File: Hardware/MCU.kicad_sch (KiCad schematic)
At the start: 28 parts, among them J3 SWD, SW1 Reset, SW2 BOOT, U4 STM32L431CBTx, U5 74AHC1G32, Y1 8M

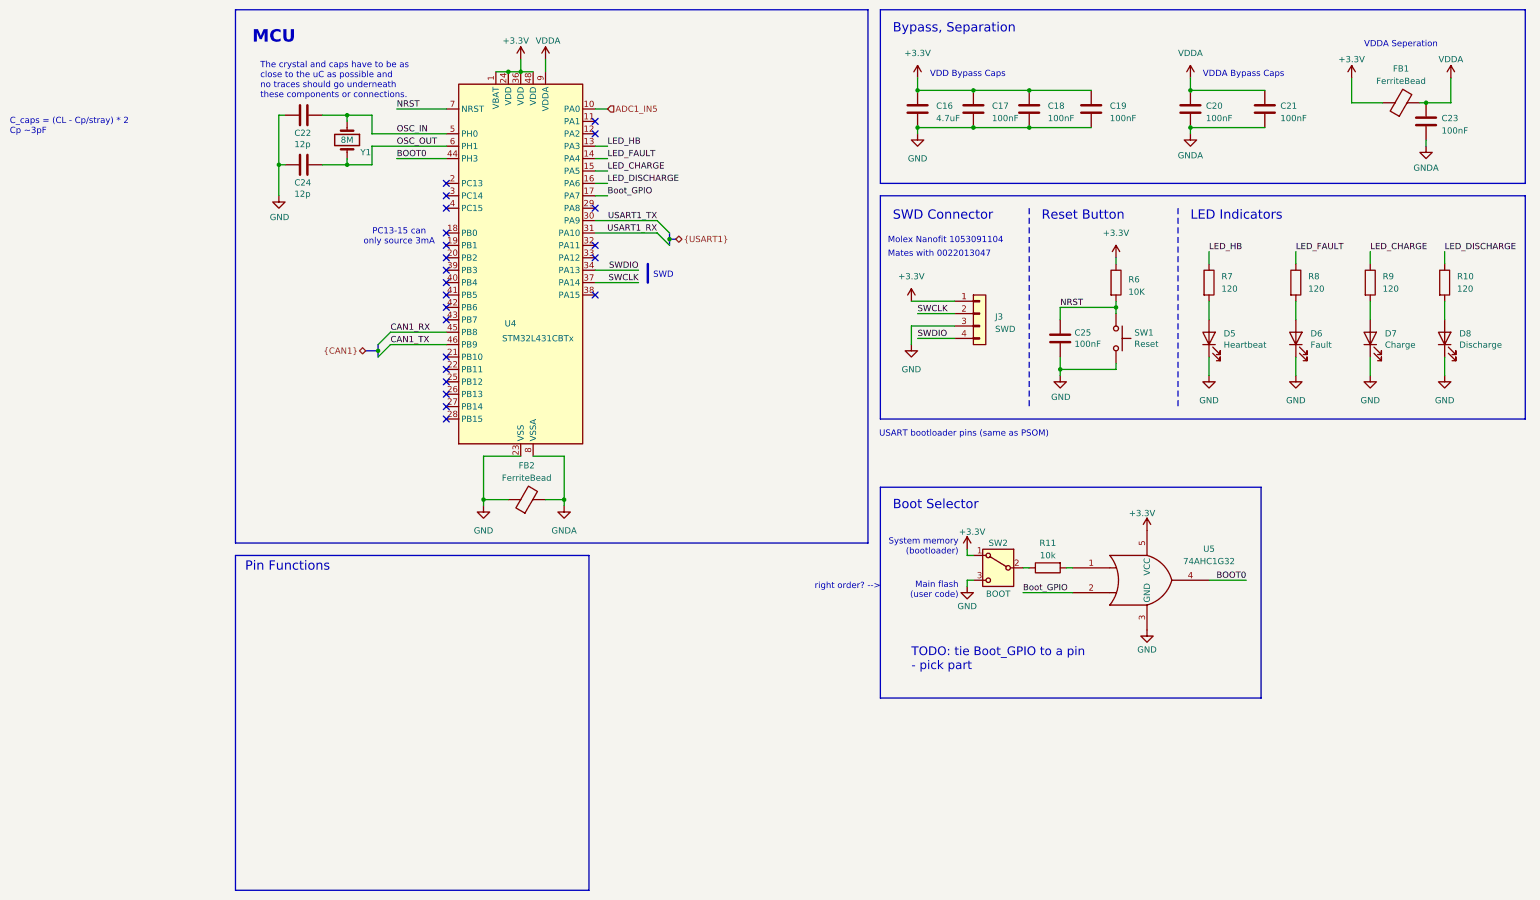
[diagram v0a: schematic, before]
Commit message: changed to 2 channel op amp, stole RPP from PSOM
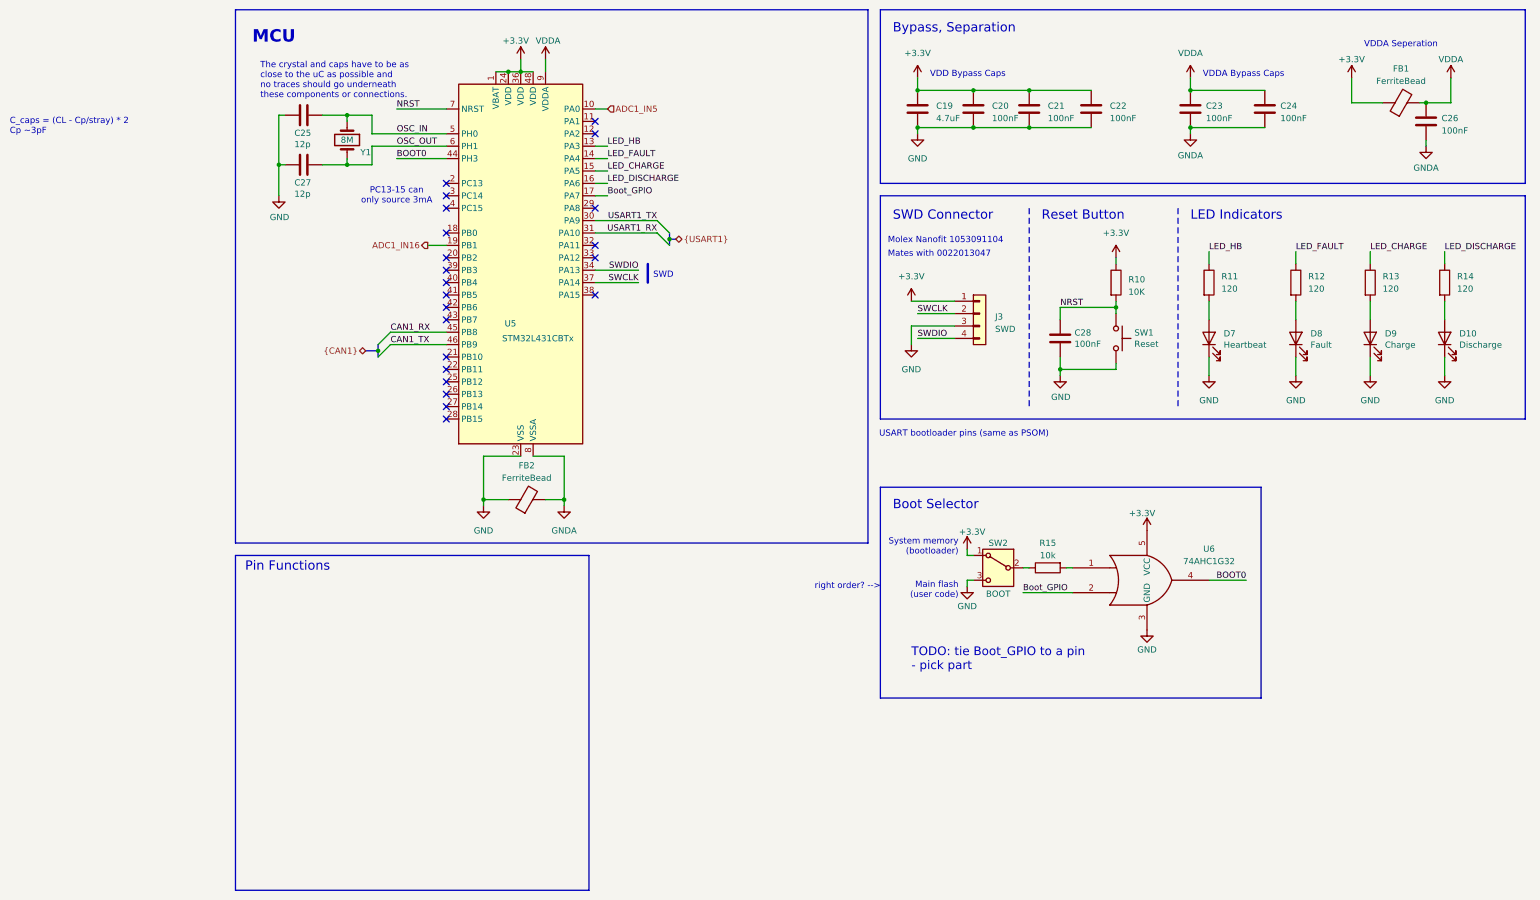
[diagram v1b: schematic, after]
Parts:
- renumbered C16 to C19, C17 to C20, C18 to C21, C19 to C22, C20 to C23, C21 to C24, C22 to C25, C23 to C26, C24 to C27, C25 to C28, D8 to D10, D5 to D7, D6 to D8, D7 to D9, R6 to R10, R7 to R11, R8 to R12, R9 to R13, R10 to R14, R11 to R15, U4 to U5, U5 to U6
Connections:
- net ADC1_IN16: now reaches U5.19 (PB1)
- no-connect marks 23 -> 22

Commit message: added voltage reference, shunt model; addressed comments
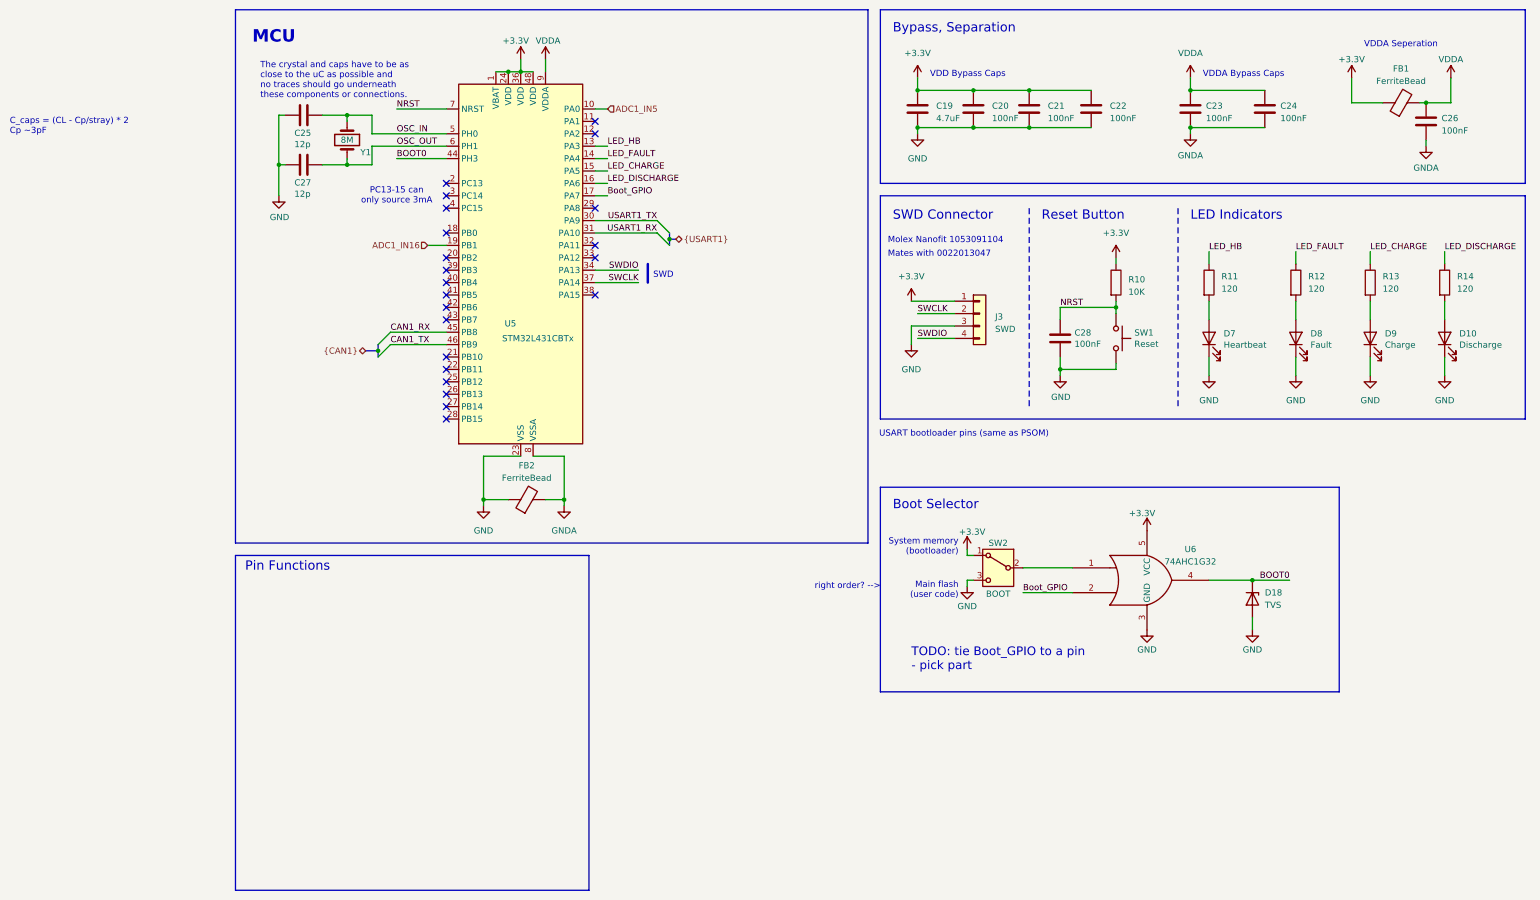
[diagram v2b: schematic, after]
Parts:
- removed R15: 10k, Resistor_SMD:R_0603_1608Metric_Pad0.98x0.95mm_HandSolder, symbol Device:R
- added D18: TVS, Diode_SMD:D_SOD-123F, symbol Device:D_Zener
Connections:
- net BOOT0: now also D18.1 (K)
- net GND: now also D18.2 (A)
- net at SW2.2 (B): now also U6.1

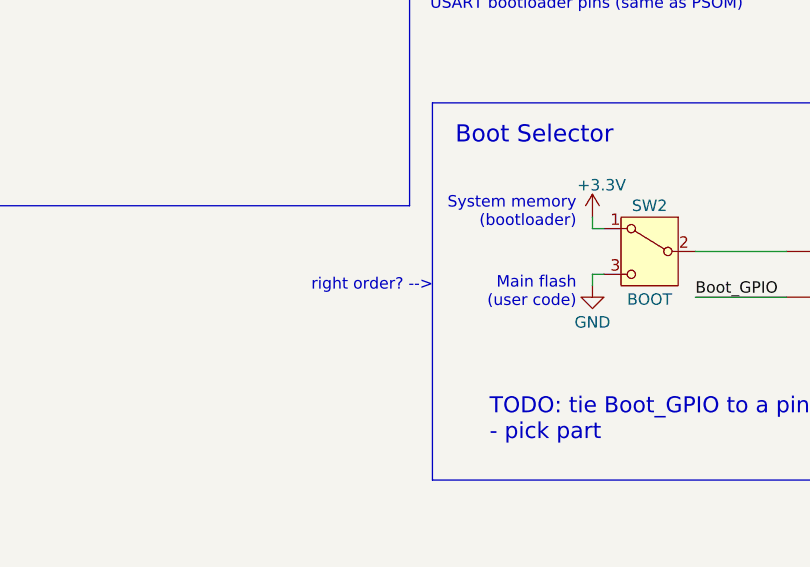
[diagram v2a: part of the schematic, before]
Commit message: added vertical usb c
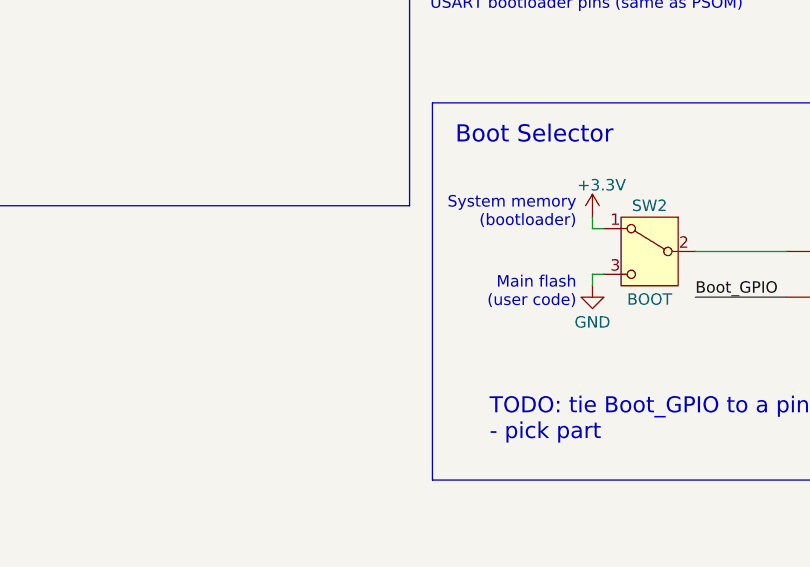
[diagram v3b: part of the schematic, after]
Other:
- note removed: "right order? -->"
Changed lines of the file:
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@@
-		)
-	)
-	(text "right order? -->"
-		(exclude_from_sim no)
-		(at 133.858 132.588 0)
-		(effects
-			(font
-				(size 1.27 1.27)
-				(color 255 30 62 1)
-			)
-			(justify left top)
 		)
 	)

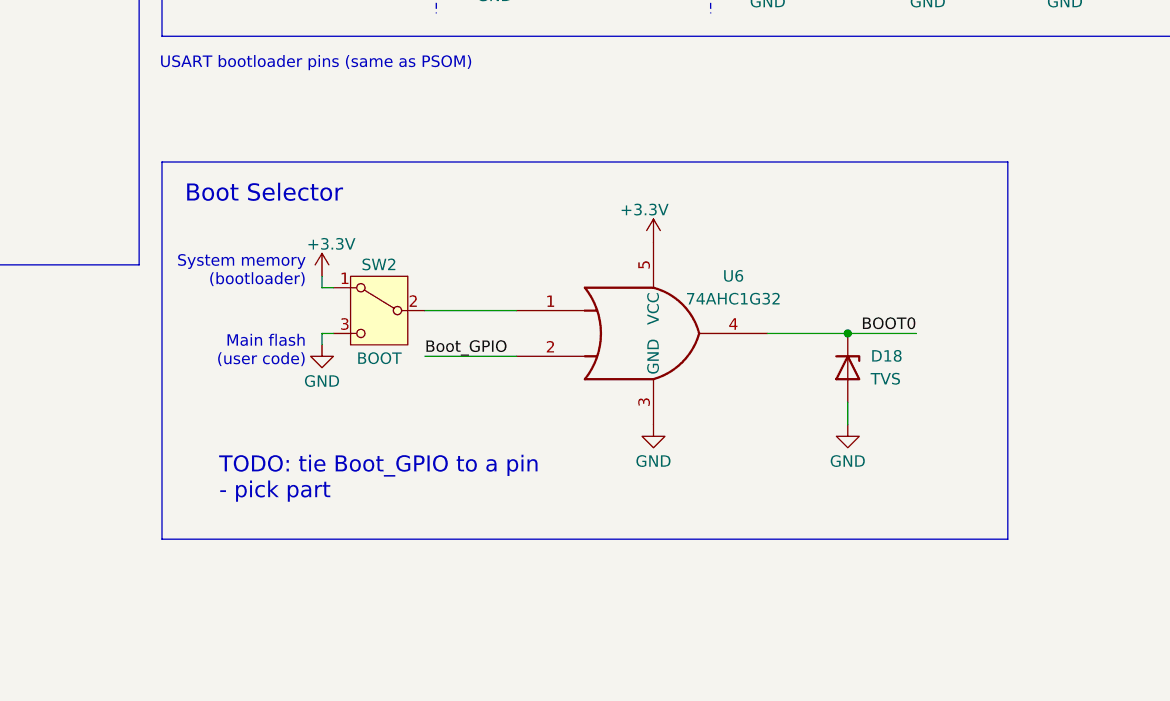
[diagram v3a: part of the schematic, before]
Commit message: renamed, added OR gate part
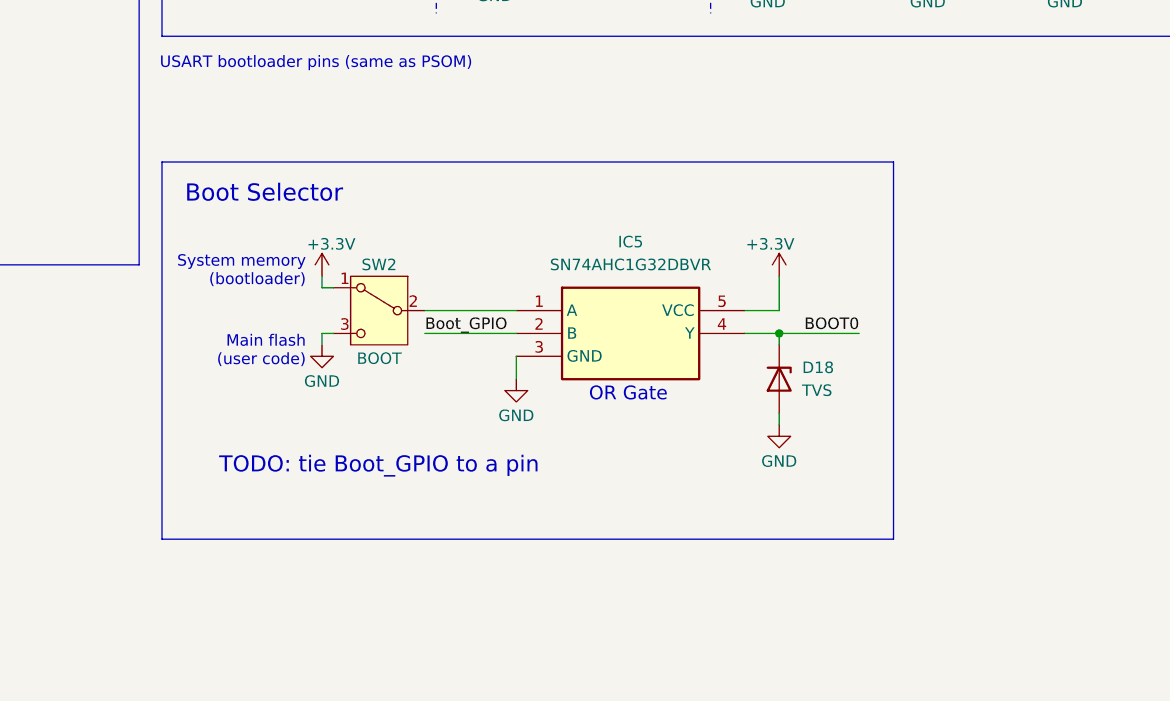
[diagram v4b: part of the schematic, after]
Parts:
- removed U6: 74AHC1G32, symbol 74xGxx:74AHC1G32
- added IC5: SN74AHC1G32DBVR, SOT95P280X145-5N, symbol SN74AHC1G32DBVR:SN74AHC1G32DBVR
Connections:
- net +3.3V: now also IC5.5 (VCC)
- net BOOT0: now also IC5.4 (Y)
- net Boot_GPIO: now also IC5.2 (B)
- net GND: now also IC5.3 (GND)
- net at SW2.2 (B): now also IC5.1 (A)
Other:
- note added: "OR Gate"
- note added: "TODO: tie Boot_GPIO to a pin"
- note removed: "TODO: tie Boot_GPIO to a pin - pick part"
- moved on the sheet: D18

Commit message: lay out lay out
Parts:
- added C29: 0.1uF, Capacitor_SMD:C_0603_1608Metric_Pad1.08x0.95mm_HandSolder, symbol Device:C
- added R15: 10k, Resistor_SMD:R_0603_1608Metric_Pad0.98x0.95mm_HandSolder, symbol Device:R
- C19: footprint Capacitor_SMD:C_0603_1608Metric_Pad1.08x0.95mm_HandSolder -> Capacitor_SMD:C_0805_2012Metric_Pad1.18x1.45mm_HandSolder; Mouser Part Number 81-GRM219R6YA475KA3D -> (none); P/N GRM219R6YA475KA73D -> 08055D475KAT4A
- IC1: renamed from IC5; footprint SOT95P280X145-5N -> Parts:SN74AHC1G32DBVR
- SW1: value Reset -> RST; footprint Button_Switch_SMD:SW_SPST_B3SL-1002P -> Parts:SW_TL3365AF180QG; Mouser Part Number 653-B3SL-1002P -> (none); P/N B3SL-1002P -> TL3365AF180QG
- renumbered D18 to D11
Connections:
- net +3.3V: now also C29.1
- net BOOT0: now also R15.1; no longer IC1.4 (Y)
- net GND: now also C29.2
- new net: IC1.4 (Y), R15.2
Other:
- moved on the sheet: D11
